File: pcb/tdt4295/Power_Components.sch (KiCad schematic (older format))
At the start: 39 parts, among them P201 690-005-299-043, U201 TPS54294, U202 TPS54325

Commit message: Finish labeling/connecting EFM32 pins
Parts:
- R211: value 1??? -> 1
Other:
- note removed: "Originalskjematikken\nviser bare 1.\nVet ikke\nstørrelsesorden"
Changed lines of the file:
@@
 P 10700 4200
 F 0 "R211" V 10493 4200 50  0000 C CNN
-F 1 "1???" V 10584 4200 50  0000 C CNN
+F 1 "1" V 10584 4200 50  0000 C CNN
 F 2 "" V 10630 4200 50  0001 C CNN
 F 3 "~" H 10700 4200 50  0001 C CNN
@@
 Text Notes 950  4750 0    50   ~ 0
 Power status LEDs & Hierarchical output
-Text Notes 10350 4650 0    50   ~ 0
-Originalskjematikken\nviser bare 1.\nVet ikke\nstørrelsesorden
-Wire Notes Line
-	10550 3950 10550 4300
-Wire Notes Line
-	10550 4300 10850 4300
-Wire Notes Line
-	10850 4300 10850 3950
-Wire Notes Line
-	10850 3950 10550 3950
 Wire Wire Line
 	8850 5100 8850 4200

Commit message: rework some efm wiring according to application notes
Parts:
- added C?: 100uF, symbol Device:C
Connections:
- wire segments 202 -> 204
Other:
- note added: "Mye av application notes viser bruk\nav ferrite bead her i stedet for en spole?"
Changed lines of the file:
@@
 Text Notes 4750 3850 0    50   ~ 0
 Ip>2.8A, Irms>2.1A
+$Comp
+L power:GND #PWR?
+U 1 1 618DCFE2
+P 1050 2300
+F 0 "#PWR?" H 1050 2050 50  0001 C CNN
+F 1 "GND" H 1055 2127 50  0000 C CNN
+F 2 "" H 1050 2300 50  0001 C CNN
+F 3 "" H 1050 2300 50  0001 C CNN
+	1    1050 2300
+	1    0    0    -1
+$EndComp
+$Comp
+L Device:C C?
+U 1 1 618DD8EF
+P 1050 2050
+F 0 "C?" H 900 2150 50  0000 L CNN
+F 1 "100uF" H 800 1950 50  0000 L CNN
+F 2 "" H 1088 1900 50  0001 C CNN
+F 3 "~" H 1050 2050 50  0001 C CNN
+	1    1050 2050
+	1    0    0    -1
+$EndComp
+Wire Wire Line
+	1050 1900 1050 1750
+Connection ~ 1050 1750
+Wire Wire Line
+	1050 2200 1050 2300
+Text Notes 1850 1450 0    50   ~ 0
+Mye av application notes viser bruk\nav ferrite bead her i stedet for en spole?
 $EndSCHEMATC

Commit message: remove analog 3v3 output
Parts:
- removed FB201: Ferrite_Bead, symbol Device:Ferrite_Bead
- removed R211: 1, symbol Device:R
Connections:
- net labels removed: +3V3A
- wire segments 204 -> 199
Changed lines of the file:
@@
-	1    0    0    -1
-$EndComp
-$Comp
-L tdt4295:+3V3A #PWR0216
-U 1 1 614DB67F
-P 10950 3950
-F 0 "#PWR0216" H 10950 3800 50  0001 C CNN
-F 1 "+3V3A" H 10965 4123 50  0000 C CNN
-F 2 "" H 10950 3950 50  0001 C CNN
-F 3 "" H 10950 3950 50  0001 C CNN
-	1    10950 3950
 	1    0    0    -1
 $EndComp
@@
 Text HLabel 2800 2350 2    50   BiDi ~ 0
 USB_D-
-$Comp
-L Device:Ferrite_Bead FB201
-U 1 1 61549D75
-P 10300 4200
-F 0 "FB201" V 10026 4200 50  0000 C CNN
-F 1 "Ferrite_Bead" V 10117 4200 50  0000 C CNN
-F 2 "" V 10230 4200 50  0001 C CNN
-F 3 "~" H 10300 4200 50  0001 C CNN
-	1    10300 4200
-	0    1    1    0
-$EndComp
-$Comp
-L Device:R R211
-U 1 1 6154B874
-P 10700 4200
-F 0 "R211" V 10493 4200 50  0000 C CNN
-F 1 "1" V 10584 4200 50  0000 C CNN
-F 2 "" V 10630 4200 50  0001 C CNN
-F 3 "~" H 10700 4200 50  0001 C CNN
-	1    10700 4200
-	0    1    1    0
-$EndComp
-Wire Wire Line
-	10550 4200 10450 4200
-Wire Wire Line
-	10850 4200 10950 4200
-Wire Wire Line
-	10950 4200 10950 3950
 Wire Wire Line
 	10000 3950 10000 4200
-Wire Wire Line
-	10000 4200 10150 4200
 $Comp
 L Device:R R209
@@
 Wire Wire Line
 	9850 4200 10000 4200
-Connection ~ 10000 4200
 Wire Wire Line
 	9850 4700 9700 4700
@@
 +3V3
 Text HLabel 1900 5450 3    50   Output ~ 0
-+3V3A
++1V8
 Text HLabel 2200 5450 3    50   Output ~ 0
-+1V8
-Text HLabel 2500 5450 3    50   Output ~ 0
 +1V0
 Wire Wire Line
@@
 $EndComp
 Wire Wire Line
-	2500 5450 2500 5050
-Wire Wire Line
-	2200 5050 2200 5450
-Wire Wire Line
-	1900 5450 1900 5050
+	2200 5450 2200 5050
+Wire Wire Line
+	1900 5050 1900 5450
 $Comp
 L power:+1V0 #PWR0208
 U 1 1 6182C82A
-P 2500 5050
-F 0 "#PWR0208" H 2500 4900 50  0001 C CNN
-F 1 "+1V0" H 2515 5223 50  0000 C CNN
-F 2 "" H 2500 5050 50  0001 C CNN
-F 3 "" H 2500 5050 50  0001 C CNN
-	1    2500 5050
-	1    0    0    -1
-$EndComp
-$Comp
-L power:+1V8 #PWR0207
-U 1 1 6182C266
 P 2200 5050
-F 0 "#PWR0207" H 2200 4900 50  0001 C CNN
-F 1 "+1V8" H 2215 5223 50  0000 C CNN
+F 0 "#PWR0208" H 2200 4900 50  0001 C CNN
+F 1 "+1V0" H 2215 5223 50  0000 C CNN
 F 2 "" H 2200 5050 50  0001 C CNN
 F 3 "" H 2200 5050 50  0001 C CNN
@@
 $EndComp
 $Comp
-L tdt4295:+3V3A #PWR0205
-U 1 1 6182B33F
+L power:+1V8 #PWR0207
+U 1 1 6182C266
 P 1900 5050
-F 0 "#PWR0205" H 1900 4900 50  0001 C CNN
-F 1 "+3V3A" H 1915 5223 50  0000 C CNN
+F 0 "#PWR0207" H 1900 4900 50  0001 C CNN
+F 1 "+1V8" H 1915 5223 50  0000 C CNN
 F 2 "" H 1900 5050 50  0001 C CNN
 F 3 "" H 1900 5050 50  0001 C CNN

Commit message: rework power regulator to only use tps54294
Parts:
- removed C202, C204, C214, C215: 22uF, symbol Device:C
- removed C206, C207, C213: 100nF, symbol Device:C
- removed C208: 3.3nF, symbol Device:C
- removed C209, C211: 1uF, symbol Device:C
- removed C210: 10uF, symbol Device:C
- removed C212: 100uF, symbol Device:C
- removed L202: 1.5uH, symbol Device:L
- removed L203: 2.2uH, symbol Device:L
- removed R203: 30.1K, symbol Device:R
- removed R204, R206, R210: 22.1K, symbol Device:R
- removed R205: 6.81K, symbol Device:R
- removed R207, R208: 100K, symbol Device:R
- removed R209: 73.2K, symbol Device:R
- removed U202: TPS54325, symbol tdt4295:TPS54325
- added C? (x2): 10uF, symbol Device:C
- added C? (x4): 100nF, symbol Device:C
- added C? (x4): 22uF, symbol Device:C
- added C?: 0.1uF, symbol Device:C
- added C?: 1uF, symbol Device:C
- added C?: 1u, symbol Device:C
- added L?: 2.2uH, symbol Device:L
- added L?: 1.5uH, symbol Device:L
- added R?: 73.2K, symbol Device:R
- added R? (x3): 22.1K, symbol Device:R
- added R?: 100K, symbol Device:R
- added R?: 6.81K, symbol Device:R
- added R?: 30.1K, symbol Device:R
- added U?: TPS54294, symbol tdt4295:TPS54294
- renumbered C201 to C?, C203 to C?, C205 to C?, C216 to C?, C217 to C?, D203 to D?, D201 to D?, D202 to D?, L201 to L?, L204 to L?, P201 to P?, R201 to R?, R202 to R?, U201 to U?
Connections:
- net labels added: R1_PG
- wire segments 199 -> 194
- no-connect marks 4 -> 8
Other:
- note removed: "Ip>2.8A, Irms>2.1A"
- note removed: "Ip>2.9A, Irms>2.1A"
- moved on the sheet: C?, L?, U?

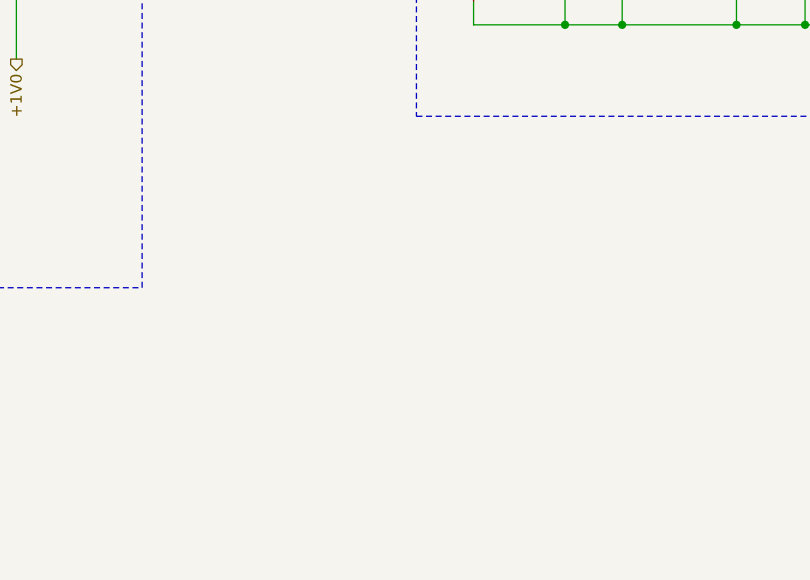
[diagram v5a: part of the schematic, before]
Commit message: add probe points for all power lines
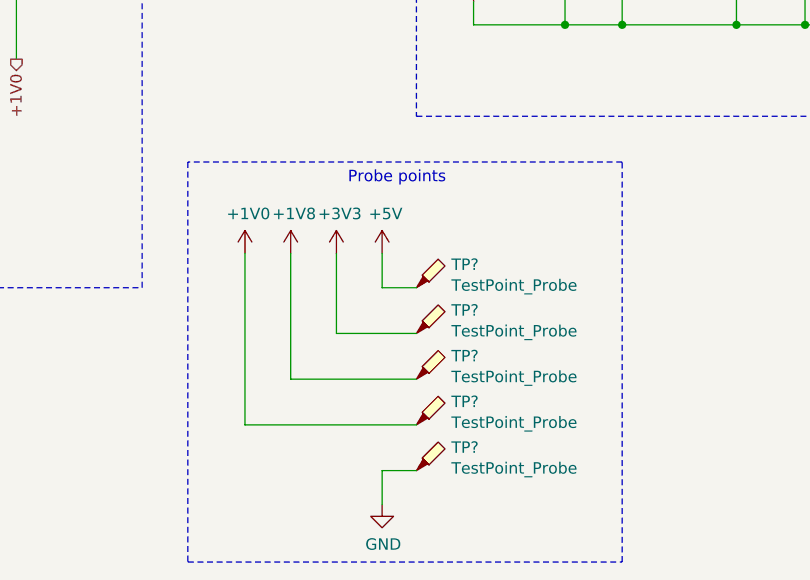
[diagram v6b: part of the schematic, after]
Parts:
- added TP? (x5): TestPoint_Probe, symbol Connector:TestPoint_Probe
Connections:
- net +1V0: now also TP?.1
- net +1V8: now also TP?.1
- net +3V3: now also TP?.1
- net +5V: now also TP?.1
- net GND: now also TP?.1
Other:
- note added: "Probe points"
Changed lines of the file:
@@
 	6700 1650 6700 1950
 Connection ~ 6700 1950
+$Comp
+L Connector:TestPoint_Probe TP?
+U 1 1 617D83E5
+P 3950 6450
+F 0 "TP?" H 4103 6551 50  0000 L CNN
+F 1 "TestPoint_Probe" H 4103 6460 50  0000 L CNN
+F 2 "" H 4150 6450 50  0001 C CNN
+F 3 "~" H 4150 6450 50  0001 C CNN
+	1    3950 6450
+	1    0    0    -1
+$EndComp
+$Comp
+L Connector:TestPoint_Probe TP?
+U 1 1 617D910C
+P 3950 6650
+F 0 "TP?" H 4103 6751 50  0000 L CNN
+F 1 "TestPoint_Probe" H 4103 6660 50  0000 L CNN
+F 2 "" H 4150 6650 50  0001 C CNN
+F 3 "~" H 4150 6650 50  0001 C CNN
+	1    3950 6650
+	1    0    0    -1
+$EndComp
+$Comp
+L Connector:TestPoint_Probe TP?
+U 1 1 617D9DC0
+P 3950 6850
+F 0 "TP?" H 4103 6951 50  0000 L CNN
+F 1 "TestPoint_Probe" H 4103 6860 50  0000 L CNN
+F 2 "" H 4150 6850 50  0001 C CNN
+F 3 "~" H 4150 6850 50  0001 C CNN
+	1    3950 6850
+	1    0    0    -1
+$EndComp
+$Comp
+L Connector:TestPoint_Probe TP?
+U 1 1 617DA131
+P 3950 7050
+F 0 "TP?" H 4103 7151 50  0000 L CNN
+F 1 "TestPoint_Probe" H 4103 7060 50  0000 L CNN
+F 2 "" H 4150 7050 50  0001 C CNN
+F 3 "~" H 4150 7050 50  0001 C CNN
+	1    3950 7050
+	1    0    0    -1
+$EndComp
+$Comp
+L Connector:TestPoint_Probe TP?
+U 1 1 617DA44A
+P 3950 7250
+F 0 "TP?" H 4103 7351 50  0000 L CNN
+F 1 "TestPoint_Probe" H 4103 7260 50  0000 L CNN
+F 2 "" H 4150 7250 50  0001 C CNN
+F 3 "~" H 4150 7250 50  0001 C CNN
+	1    3950 7250
+	1    0    0    -1
+$EndComp
+$Comp
+L power:+5V #PWR?
+U 1 1 617E7DF6
+P 3800 6300
+F 0 "#PWR?" H 3800 6150 50  0001 C CNN
+F 1 "+5V" H 3815 6473 50  0000 C CNN
+F 2 "" H 3800 6300 50  0001 C CNN
+F 3 "" H 3800 6300 50  0001 C CNN
+	1    3800 6300
+	1    0    0    -1
+$EndComp
+Wire Wire Line
+	3800 6300 3800 6450
+Wire Wire Line
+	3800 6450 3950 6450
+$Comp
+L power:+3V3 #PWR?
+U 1 1 61800EE5
+P 3600 6300
+F 0 "#PWR?" H 3600 6150 50  0001 C CNN
+F 1 "+3V3" H 3615 6473 50  0000 C CNN
+F 2 "" H 3600 6300 50  0001 C CNN
+F 3 "" H 3600 6300 50  0001 C CNN
+	1    3600 6300
+	1    0    0    -1
+$EndComp
+Wire Wire Line
+	3600 6300 3600 6650
+Wire Wire Line
+	3600 6650 3950 6650
+$Comp
+L power:+1V8 #PWR?
+U 1 1 6180C15B
+P 3400 6300
+F 0 "#PWR?" H 3400 6150 50  0001 C CNN
+F 1 "+1V8" H 3415 6473 50  0000 C CNN
+F 2 "" H 3400 6300 50  0001 C CNN
+F 3 "" H 3400 6300 50  0001 C CNN
+	1    3400 6300
+	1    0    0    -1
+$EndComp
+Wire Wire Line
+	3400 6300 3400 6850
+Wire Wire Line
+	3400 6850 3950 6850
+$Comp
+L power:+1V0 #PWR?
+U 1 1 61817BCE
+P 3200 6300
+F 0 "#PWR?" H 3200 6150 50  0001 C CNN
+F 1 "+1V0" H 3215 6473 50  0000 C CNN
+F 2 "" H 3200 6300 50  0001 C CNN
+F 3 "" H 3200 6300 50  0001 C CNN
+	1    3200 6300
+	1    0    0    -1
+$EndComp
+Wire Wire Line
+	3200 6300 3200 7050
+Wire Wire Line
+	3200 7050 3950 7050
+$Comp
+L power:GND #PWR?
+U 1 1 61823BA4
+P 3800 7400
+F 0 "#PWR?" H 3800 7150 50  0001 C CNN
+F 1 "GND" H 3805 7227 50  0000 C CNN
+F 2 "" H 3800 7400 50  0001 C CNN
+F 3 "" H 3800 7400 50  0001 C CNN
+	1    3800 7400
+	1    0    0    -1
+$EndComp
+Wire Wire Line
+	3800 7400 3800 7250
+Wire Wire Line
+	3800 7250 3950 7250
+Wire Notes Line
+	2950 5900 2950 7650
+Wire Notes Line
+	2950 7650 4850 7650
+Wire Notes Line
+	4850 7650 4850 5900
+Wire Notes Line
+	4850 5900 2950 5900
+Text Notes 3650 6000 0    50   ~ 0
+Probe points
 $EndSCHEMATC

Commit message: rework MCU pinning
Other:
- note removed: "Ip>3.5A Irms>3.1A"
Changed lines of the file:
@@
 Text Notes 950  4750 0    50   ~ 0
 Power status LEDs & Hierarchical output
-Text Notes 9050 1150 0    50   ~ 0
-Ip>3.5A Irms>3.1A
 NoConn ~ 1350 1500
 $Comp
@@
 Wire Wire Line
 	5450 1200 8300 1200
-Text GLabel 8200 2150 2    50   Input ~ 0
+Text GLabel 8200 2150 2    50   Output ~ 0
 R1_PG
 Wire Wire Line

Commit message: minor schematic fixes
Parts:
- removed L?: BKP2125HS221-T, BKP2125_TAY, symbol 2021-09-07_12-32-16:BKP2125HS221-T
- added FB?: Ferrite_Bead, symbol Device:Ferrite_Bead
- gave numbers to parts that had none: 42
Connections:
- net +5V: now also FB?.1
- net at C201.1, D203.5 (VP), P201.1: now also FB?.2
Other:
- note removed: "Mye av application notes viser bruk\nav ferrite bead her i stedet for en spole?"
